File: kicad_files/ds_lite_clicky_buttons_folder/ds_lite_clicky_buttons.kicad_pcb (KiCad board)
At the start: 2 copper layers, 23.9 x 24.5 mm, 9 parts, among them P00 TestPoint, P01 TestPoint, SW1 SW_Push, SW2 SW_Push, SW3 SW_Push, SW4 SW_Push

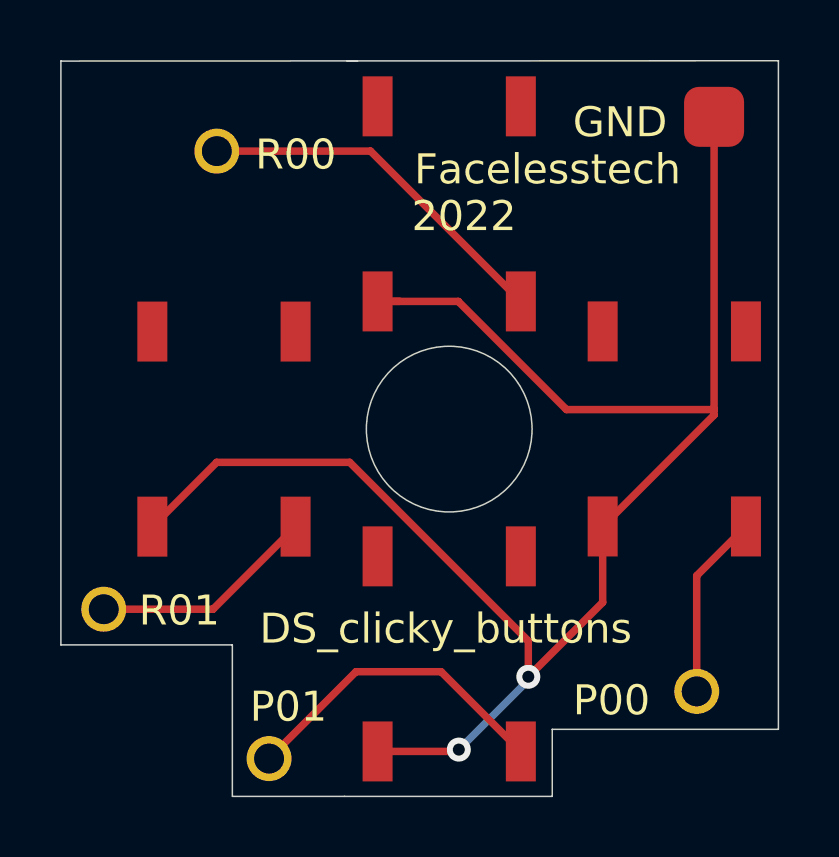
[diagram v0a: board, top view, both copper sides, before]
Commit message: Update d-pad PCB
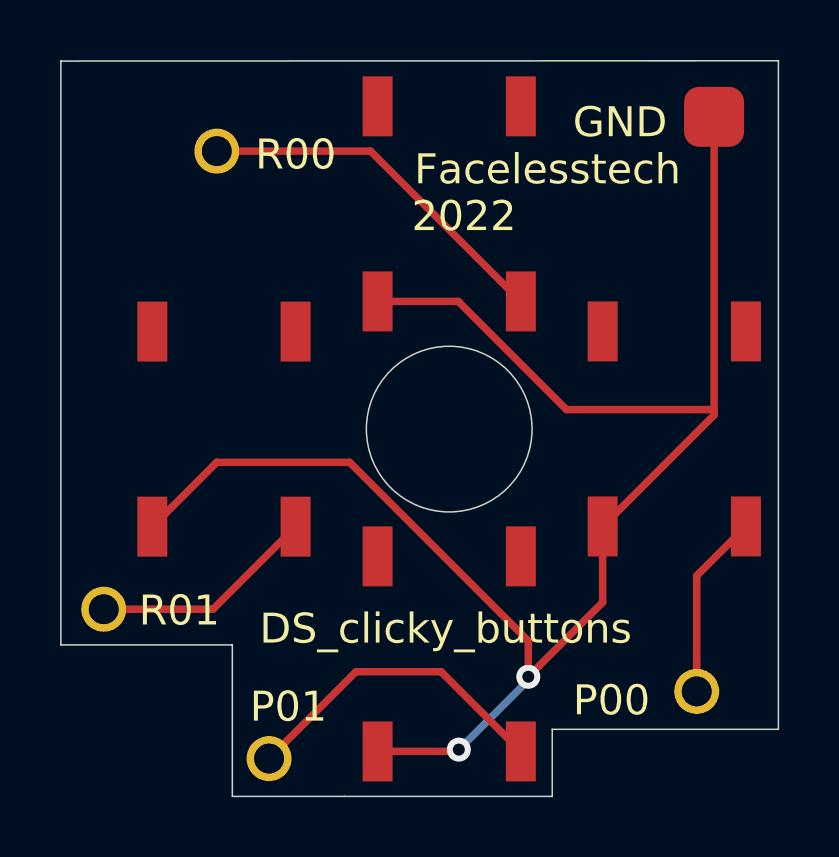
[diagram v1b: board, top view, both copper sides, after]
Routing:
- net Net-(SW1-Pad1): track 57.8 -> 57.1 mm
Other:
- outline, holes or cut-outs redrawn
- net class Default removed
